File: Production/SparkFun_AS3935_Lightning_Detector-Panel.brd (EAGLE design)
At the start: 123.2 x 175 mm, 1395 parts, among them U1 AS3935, U10 AS3935, U11 AS3935, U12 AS3935, U13 AS3935, U14 AS3935, U15 AS3935, U16 AS3935, U17 AS3935, U18 AS3935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

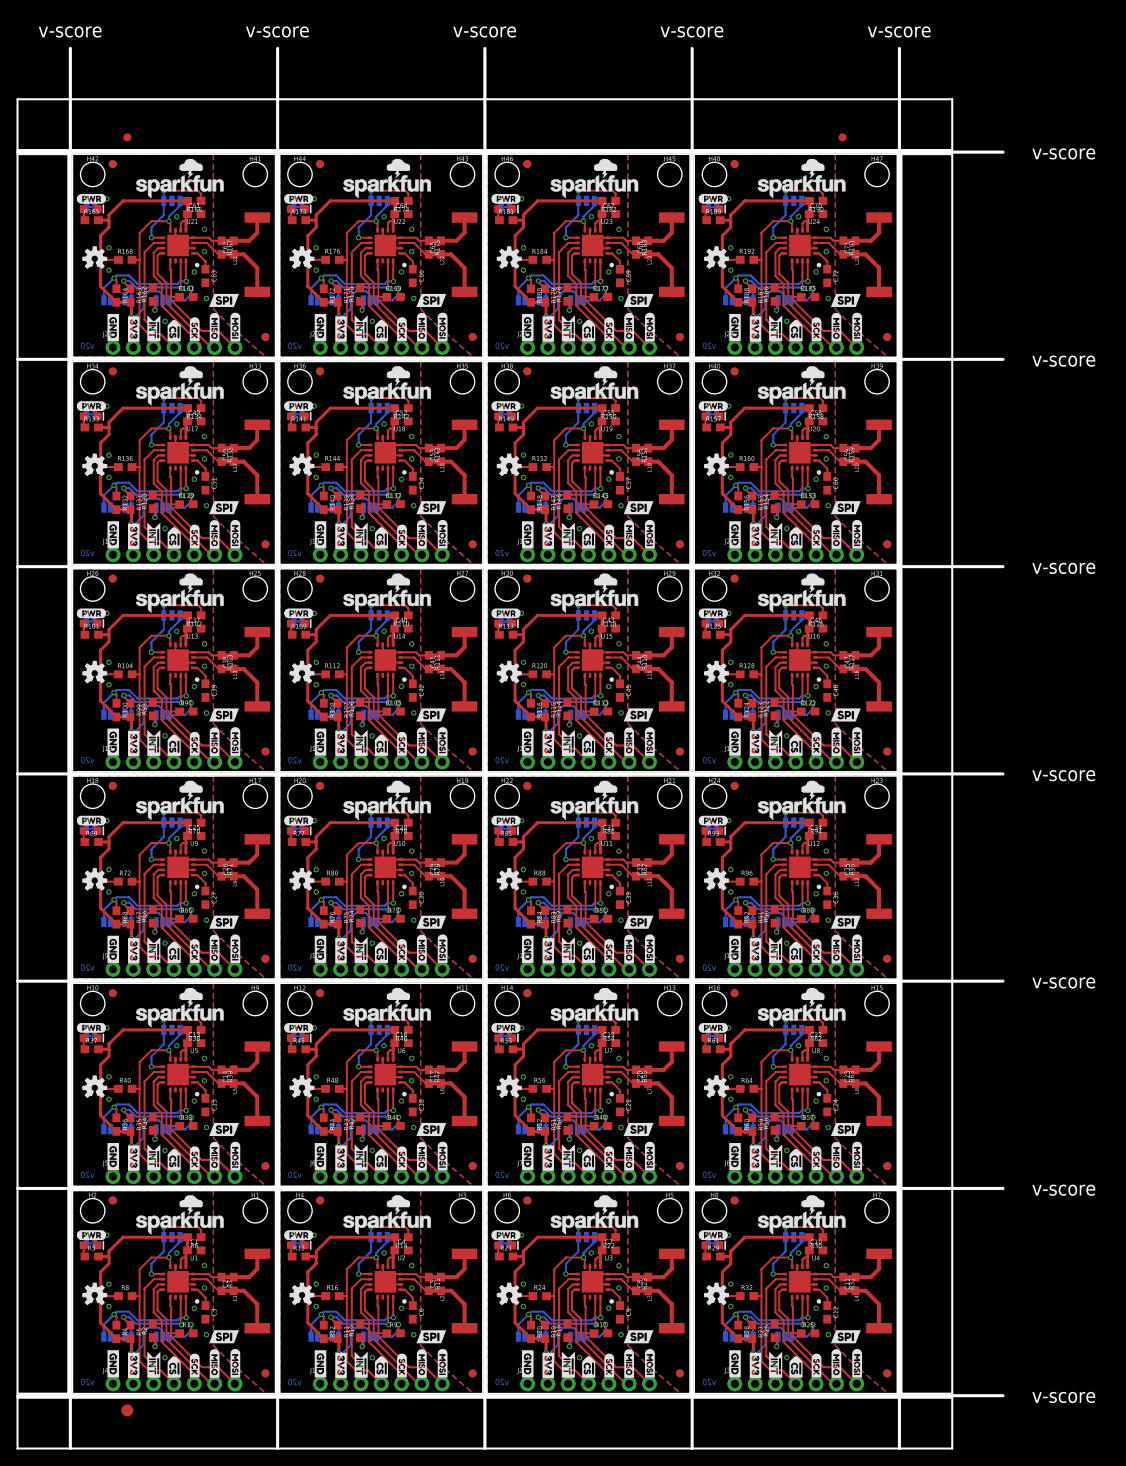
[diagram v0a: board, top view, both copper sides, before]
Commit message: Fixes interrupt label and repanelizes product
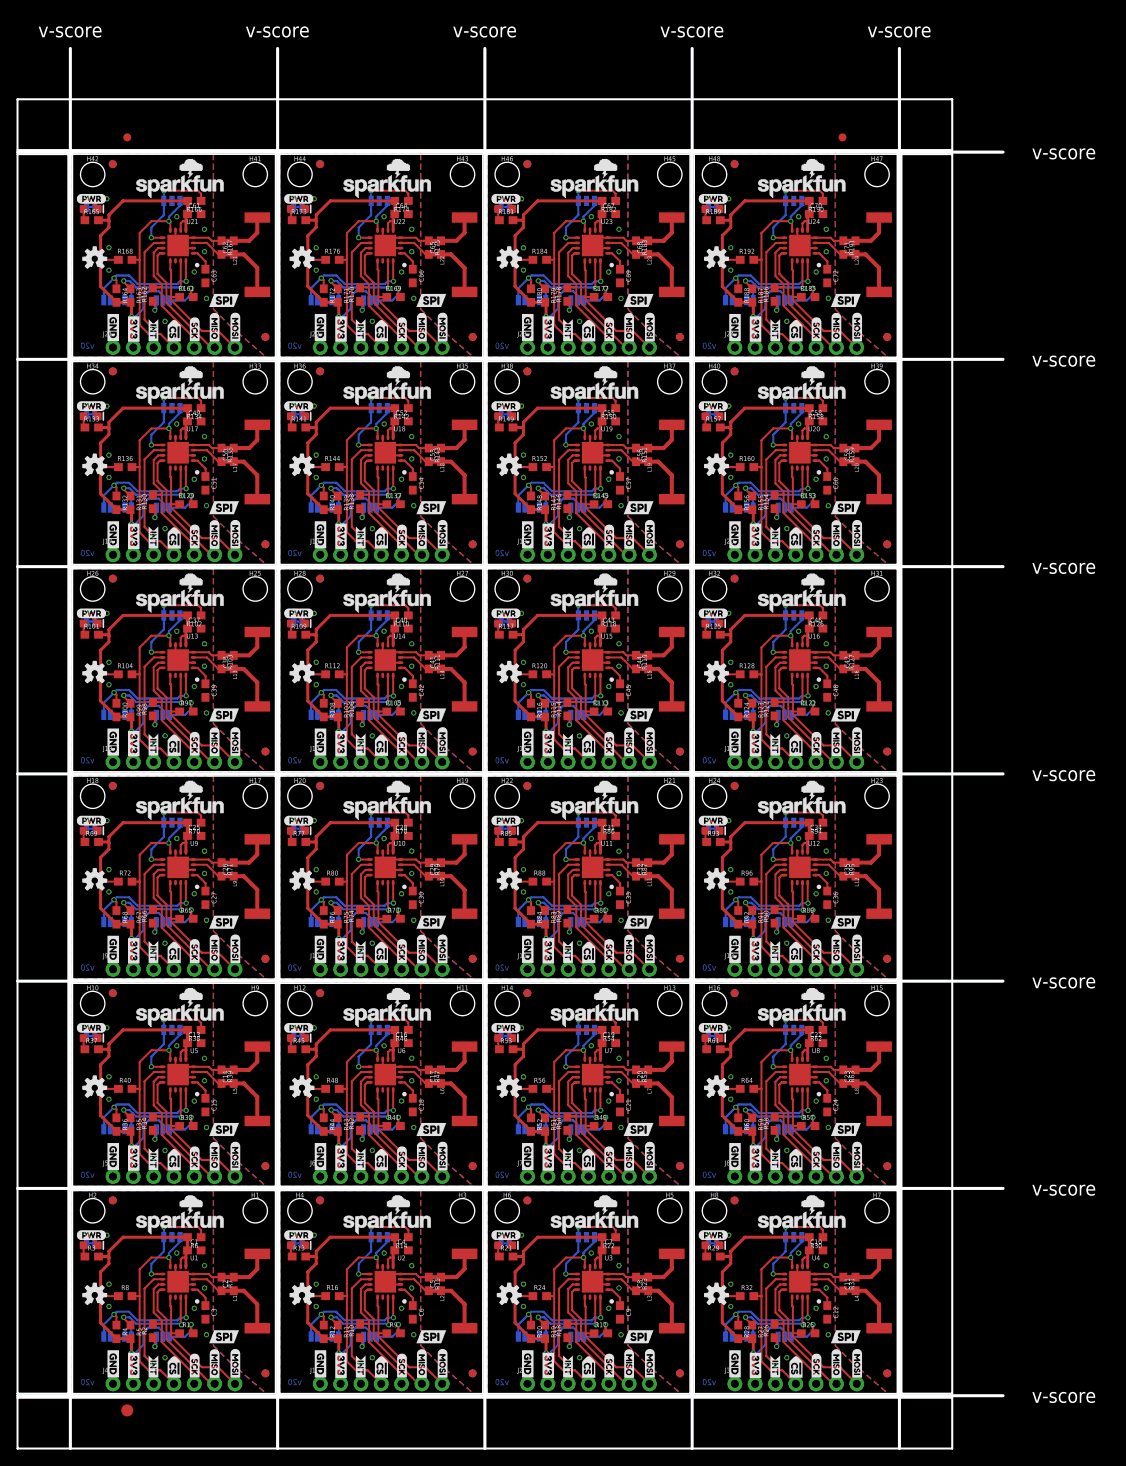
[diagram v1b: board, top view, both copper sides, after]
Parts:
- U$111, U$140, U$169, U$198, U$227, U$256, U$285, U$314, U$343, U$372, U$401, U$430, U$459, U$488, U$517, U$53, U$546, U$575, U$604, U$633, U$662, U$691, U$82: device INT:#INT0 -> DataLines:SPI1
- U$112, U$141, U$170, U$199, U$228, U$257, U$286, U$315, U$344, U$373, U$402, U$431, U$460, U$489, U$518, U$54, U$547, U$576, U$605, U$634, U$663, U$692, U$83: device INT:#INT0 -> i2c_EN:I#C_EN0
- U$113, U$142, U$171, U$200, U$229, U$258, U$287, U$316, U$345, U$374, U$403, U$432, U$461, U$490, U$519, U$548, U$55, U$577, U$606, U$635, U$664, U$693, U$84: device DataLines:SPI1 -> CS and SI:CS0
- U$114, U$143, U$172, U$201, U$230, U$259, U$288, U$317, U$346, U$375, U$404, U$433, U$462, U$491, U$520, U$549, U$56, U$578, U$607, U$636, U$665, U$694, U$85: device i2c_EN:I#C_EN0 -> CS and SI:SI1
- U$115, U$144, U$173, U$202, U$231, U$260, U$289, U$318, U$347, U$376, U$405, U$434, U$463, U$492, U$521, U$550, U$57, U$579, U$608, U$637, U$666, U$695, U$86: device CS and SI:CS0 -> buzzard_labels:INT0
- U$116, U$145, U$174, U$203, U$232, U$261, U$290, U$319, U$348, U$377, U$406, U$435, U$464, U$493, U$522, U$551, U$58, U$580, U$609, U$638, U$667, U$696, U$87: device CS and SI:SI1 -> buzzard_labels:INT0
- U$13, U$14: device INT:#INT0 -> buzzard_labels:INT0
- moved U$199 17.0 mm to (67.2, 47.6), turned to 0 degrees
- moved U$141 17.0 mm to (15.4, 47.6), turned to 0 degrees
- moved U$170 17.0 mm to (41.3, 47.6), turned to 0 degrees
- moved U$431 17.0 mm to (67.2, 99.4), turned to 0 degrees
- moved U$547 17.0 mm to (67.2, 125.3), turned to 0 degrees
- moved U$663 17.0 mm to (67.2, 151.2), turned to 0 degrees
- moved U$83 17.0 mm to (67.2, 21.7), turned to 0 degrees
- moved U$228 17.0 mm to (93.1, 47.6), turned to 0 degrees
- moved U$373 17.0 mm to (15.4, 99.4), turned to 0 degrees
- moved U$402 17.0 mm to (41.3, 99.4), turned to 0 degrees
- moved U$489 17.0 mm to (15.4, 125.3), turned to 0 degrees
- moved U$518 17.0 mm to (41.3, 125.3), turned to 0 degrees
- moved U$54 17.0 mm to (41.3, 21.7), turned to 0 degrees
- moved U$605 17.0 mm to (15.4, 151.2), turned to 0 degrees
- moved U$634 17.0 mm to (41.3, 151.2), turned to 0 degrees
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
